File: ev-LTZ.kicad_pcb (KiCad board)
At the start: 2 copper layers, 50 x 100 mm, 41 parts, among them P1 VIN+, P2 CONN_01X02, P3 VH-, P4 VH+, P5 SENSE-, P6 SENSE+, P7 VIN-, Q1 BD139, U1 LT1013N8

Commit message: pcb
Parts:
- removed C8: 1uF, Capacitors_THT:CP_Radial_Tantal_D5.0mm_P5.00mm
- removed C9: .1uF, Capacitors_THT:C_Rect_L7.2mm_W2.5mm_P5.00mm_FKS2_FKP2_MKS2_MKP2
- removed D4, D5, D7: D_TVS, Diodes_THT:D_DO-15_P10.16mm_Horizontal
- C10, C5: value 1uF -> 47uF
- moved C4 83.9 mm to (137.1, 53.4), turned to 180 degrees
- moved C10 78.5 mm to (137.1, 58.0), turned to 180 degrees
- moved P2 77.3 mm to (134.0, 128.9), turned to 90 degrees
- moved TH1 63.5 mm to (142.9, 120.7), turned to 270 degrees
- moved D6 47.2 mm to (133.0, 87.8), turned to 270 degrees
- moved P4 42.5 mm to (134.0, 104.0)
- moved P6 38.5 mm to (175.9, 91.4)
- moved R4 36.8 mm to (168.9, 121.9)
- moved P7 33.9 mm to (176.5, 111.1)
- moved C5 29.6 mm to (155.0, 106.9), turned to 0 degrees
- moved P3 28.2 mm to (134.0, 116.8)
- moved P5 24.8 mm to (175.9, 78.7)
- moved P1 24.1 mm to (176.5, 123.8)
- moved W2 19.7 mm to (149.8, 129.0)
- moved D3 19.5 mm to (160.0, 126.4), turned to 0 degrees
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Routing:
- net Net-(C7-Pad1): track 30.6 -> 190.2 mm
- net Net-(LTZ1000-1-Pad4): track 75.2 -> 138.4 mm
- net Net-(C10-Pad1): track 98.5 -> 41.0 mm
- net /SENSE+: track 148.4 -> 203.9 mm
- net /VH-: track 134.0 -> 87.9 mm
- net Net-(C5-Pad1): track 63.0 -> 32.2 mm
- net /TSENSE: track 92.8 -> 114.6 mm
- net Net-(C2-Pad1): track 32.9 -> 48.1 mm
- net Net-(D2-Pad2): track 11.6 -> 24.6 mm
- net Net-(C1-Pad2): track 57.6 -> 44.7 mm
- net Net-(P2-Pad2): track 0.11 -> 10.2 mm
- net Net-(P2-Pad1): track 0.11 -> 8.94 mm
- net GND: track 198.4 -> 191.5 mm
- net /VH+: track 11.8 -> 6.62 mm
- net Net-(C3-Pad1): track 68.5 -> 71.8 mm
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
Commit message: V00 of pcb
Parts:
- moved D2 34.9 mm to (172.5, 99.7), turned to 180 degrees
- moved R9 16.2 mm to (159.6, 79.6), turned to 180 degrees
- moved LTZ1000-1 7.84 mm to (169.4, 57.7), turned to 270 degrees
- moved D1 6.36 mm to (146.7, 53.3)
- moved Q1 5.73 mm to (141.7, 57.9)
- moved R2 3.69 mm to (167.8, 118.6)
- moved W2 2.90 mm to (152.7, 129.0)
- moved R4 1.55 mm to (167.6, 122.8)
- moved P7 0.51 mm to (176.0, 111.1)
- moved P6 0.28 mm to (176.0, 91.2)
- moved P1 0.25 mm to (176.3, 123.8)
- moved R6 0.15 mm to (135.3, 82.5)
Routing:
- net Net-(C7-Pad1): track 190.2 -> 35.2 mm
- net Net-(LTZ1000-1-Pad4): track 138.4 -> 95.0 mm
- net Net-(C2-Pad1): track 48.1 -> 87.1 mm
- net GND: track 191.5 -> 160.1 mm
- net Net-(C3-Pad1): track 71.8 -> 101.3 mm
- net Net-(D2-Pad2): track 24.6 -> 4.37 mm
- net /SENSE+: track 203.9 -> 184.9 mm
- net Net-(C1-Pad2): track 44.7 -> 59.0 mm
- net /VH-: track 87.9 -> 81.9 mm
- net /HEAT: track 5.78 -> 11.0 mm
- net Net-(C5-Pad1): track 32.2 -> 36.9 mm
- net /TSENSE: track 114.6 -> 118.6 mm
- net Net-(C10-Pad1): track 41.0 -> 43.4 mm
- net Net-(D1-Pad2): track 20.2 -> 22.0 mm
- net Net-(C7-Pad2): track 32.8 -> 34.5 mm

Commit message: finish pcb
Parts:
- moved P3 49.8 mm to (133.6, 67.1)
- moved P4 26.3 mm to (133.6, 77.7)
- moved D6 23.3 mm to (137.7, 65.0)
- moved W1 11.0 mm to (145.8, 70.6)
- moved R6 9.34 mm to (143.3, 87.4)
- moved C1 8.32 mm to (138.2, 86.3)
- moved R7 6.88 mm to (138.2, 102.1)
- moved C4 5.61 mm to (138.2, 58.9), turned to 90 degrees
- moved R9 4.70 mm to (159.6, 84.3)
- moved P2 4.45 mm to (134.0, 124.5)
- moved R4 4.40 mm to (170.7, 126.0)
- moved TH1 4.32 mm to (142.9, 125.0)
- moved D3 3.68 mm to (160.0, 130.0)
- moved D2 3.06 mm to (174.8, 101.7)
- moved C10 3.02 mm to (136.7, 61.0)
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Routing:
- net /VH-: track 81.9 -> 25.2 mm
- net Net-(C10-Pad1): track 43.4 -> 19.1 mm
- net Net-(LTZ1000-1-Pad4): track 95.0 -> 118.7 mm
- net Net-(C7-Pad2): track 34.5 -> 20.4 mm
- net Net-(C3-Pad1): track 101.3 -> 110.7 mm
- net Net-(C2-Pad1): track 87.1 -> 79.1 mm
- net /SENSE+: track 184.9 -> 192.5 mm
- net Net-(C1-Pad2): track 59.0 -> 64.5 mm
- net /TSENSE: track 118.6 -> 115.1 mm
- net Net-(C1-Pad1): track 6.49 -> 3.08 mm
- net Net-(C5-Pad1): track 36.9 -> 33.7 mm
- net GND: track 160.1 -> 162.4 mm
- net Net-(D2-Pad2): track 4.37 -> 6.65 mm
- net /HEAT: track 11.0 -> 13.1 mm
- net /VH+: track 6.62 -> 5.12 mm
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- added copper zone on B.Cu, net /SENSE+
- added copper zone on F.Cu, net /SENSE+
- added copper zone on B.Cu, net /TSENSE
- added copper zone on B.Cu, net /VH-
- added copper zone on B.Cu, net /VIN+
- added copper zone on F.Cu, net GND
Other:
- net class Default: trace_width 0.508 -> 0.762
- net class Power added: clearance 0.2, trace_width 1.016, via_dia 0.6, via_drill 0.4

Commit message: change footprint
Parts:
- removed R4.2: 25k, Resistors_THT:R_Axial_DIN0614_L14.3mm_D5.7mm_P15.24mm_Horizontal
- R1, R2, R3, R5: footprint Resistors_THT:R_Axial_DIN0614_L14.3mm_D5.7mm_P15.24mm_Horizontal -> Resistors_THT:R_Axial_DIN0617_L17.0mm_D6.0mm_P20.32mm_Horizontal
- R4.1: value 25k -> 12k; footprint Resistors_THT:R_Axial_DIN0614_L14.3mm_D5.7mm_P15.24mm_Horizontal -> Resistors_THT:R_Axial_DIN0617_L17.0mm_D6.0mm_P20.32mm_Horizontal
- moved R1 60.6 mm to (189.2, 83.8)
- moved R4.1 9.16 mm to (133.1, 136.7)
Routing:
- net Net-(LTZ1000-1-Pad4): track 118.7 -> 42.4 mm
- net /TSENSE: track 115.1 -> 108.8 mm

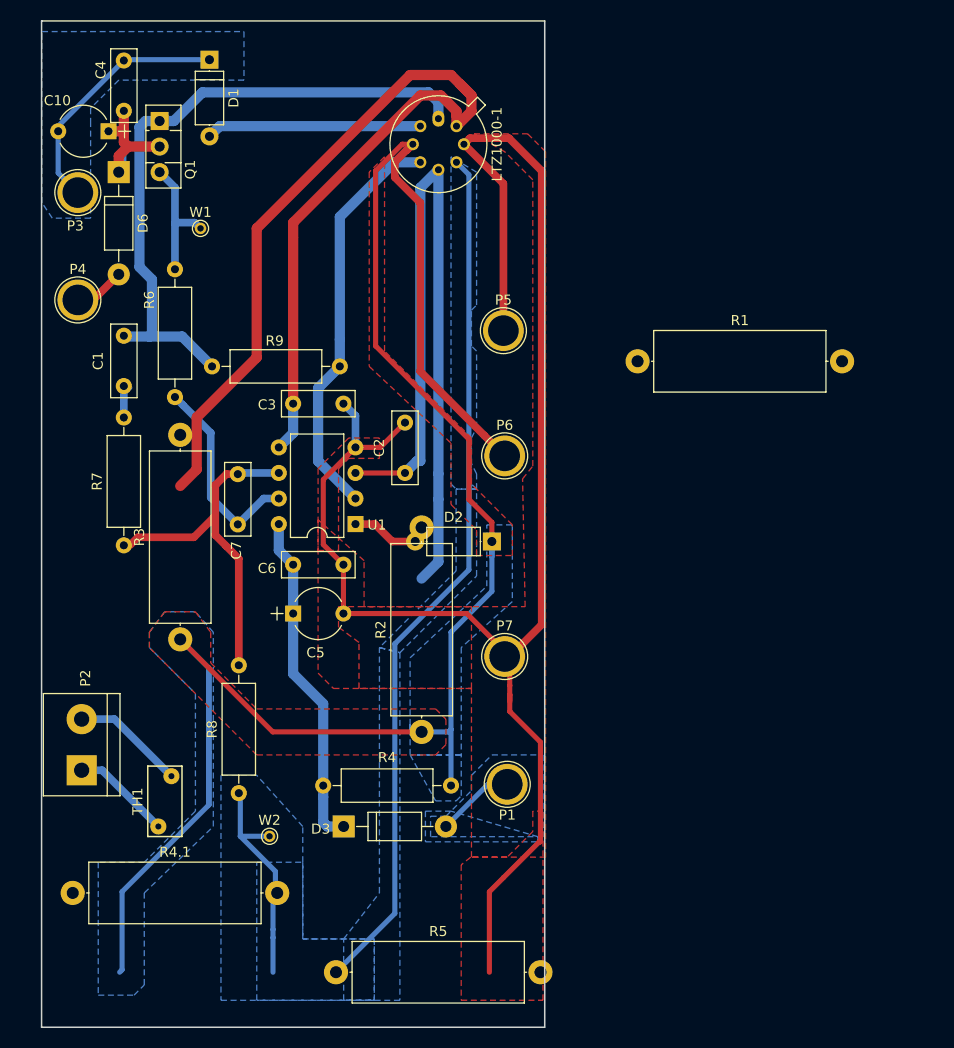
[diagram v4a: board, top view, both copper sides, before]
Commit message: modify layout
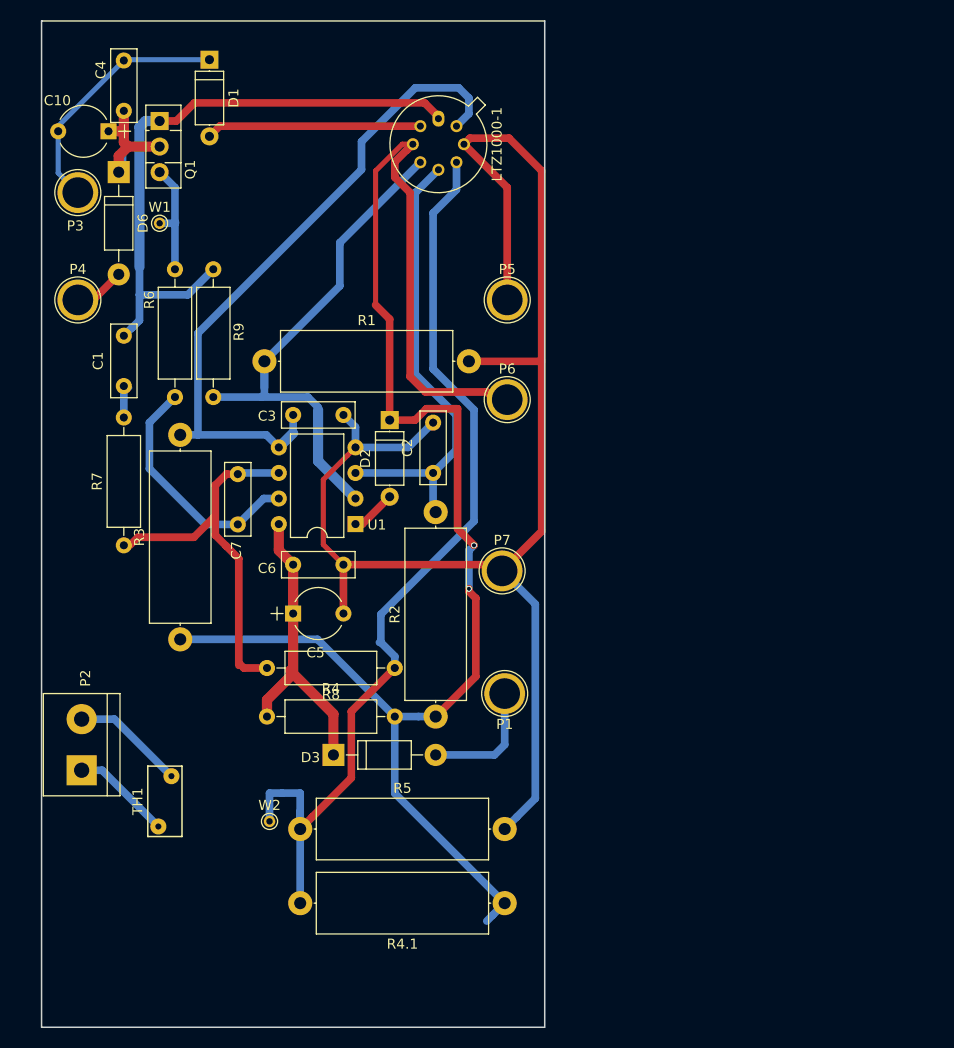
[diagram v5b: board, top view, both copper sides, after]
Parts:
- moved R4.1 42.9 mm to (176.0, 137.7), turned to 180 degrees
- moved R1 37.1 mm to (152.1, 83.8)
- moved R8 19.9 mm to (165.1, 114.3), turned to 180 degrees
- moved D2 15.8 mm to (164.6, 89.7), turned to 270 degrees
- moved R5 14.7 mm to (155.7, 130.3)
- moved R9 12.9 mm to (147.1, 87.4), turned to 90 degrees
- moved P1 9.02 mm to (176.0, 116.8)
- moved R4 8.85 mm to (165.1, 119.1)
- moved P7 8.51 mm to (175.8, 104.6)
- moved D3 7.18 mm to (159.0, 122.9)
- moved P6 5.59 mm to (176.3, 87.6)
- moved W1 4.10 mm to (141.7, 70.1)
- moved P5 3.07 mm to (176.3, 77.7)
- moved C2 2.79 mm to (168.9, 94.9)
- moved R2 2.07 mm to (169.2, 119.1)
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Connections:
- net /TSENSE renamed /TSENSE_B
- net Net-(C1-Pad2) renamed /HEATER+
- net Net-(C10-Pad1) renamed /VCC
- net Net-(C2-Pad1) renamed /TCOMP
- net Net-(C3-Pad1) renamed /TSENSE_C
- net Net-(D1-Pad2) renamed /HEATER-
- net Net-(D2-Pad2) renamed /CURRENT_OUT
- net Net-(LTZ1000-1-Pad4) renamed /ZENER-
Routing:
- net /TSENSE_C: track 110.7 -> 66.6 mm
- net /TCOMP: track 79.1 -> 45.4 mm
- net /SENSE+: track 192.5 -> 160.7 mm, vias 0 -> 2
- net /ZENER-: track 42.4 -> 55.8 mm
- net /TSENSE_B: track 108.8 -> 95.9 mm
- net GND: track 162.4 -> 151.2 mm
- net Net-(C7-Pad2): track 20.4 -> 24.4 mm
- net Net-(C7-Pad1): track 35.4 -> 38.4 mm
- net /HEATER+: track 64.5 -> 61.6 mm
- net Net-(C5-Pad1): track 33.7 -> 31.1 mm
- net /VIN+: track 9.72 -> 12.4 mm
- net /CURRENT_OUT: track 6.65 -> 4.52 mm
- net /HEAT: track 13.1 -> 11.9 mm
- added copper zone on B.Cu, net /TSENSE
- removed copper zone on B.Cu, net /SENSE+
- removed copper zone on F.Cu, net /SENSE+
- removed copper zone on B.Cu, net /TSENSE_B
- removed copper zone on B.Cu, net /VH-
- removed copper zone on B.Cu, net /VIN+
- removed copper zone on F.Cu, net GND

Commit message: improve traces
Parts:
- added R4.2: 25k, Resistors_THT:R_Axial_DIN0617_L17.0mm_D6.0mm_P20.32mm_Horizontal, F.Cu at (155.7, 120.7)
- added REF**: 1pin, Connectors:1pin, F.Cu at (157.4, 67.6)
- added REF**: 1pin, Connectors:1pin, F.Cu at (175.4, 60.2)
- C10, C5: footprint Capacitors_THT:CP_Radial_Tantal_D5.0mm_P5.00mm -> Capacitors_THT:CP_Radial_D8.0mm_P5.00mm
- P2: value CONN_01X02 -> TEMP NTC; footprint Connectors:bornier2 -> Connectors_Samtec:SL-102-X-XX_1x02
- P5, P6: footprint Connectors:1pin -> Measurement_Points:Measurement_Point_Round-TH_Big
- R4.1: value 12k -> 25k
- moved P3 77.6 mm to (136.0, 144.7)
- moved P4 69.0 mm to (149.7, 144.8)
- moved C10 54.9 mm to (138.0, 115.8)
- moved D6 54.3 mm to (140.5, 119.3)
- moved P7 40.3 mm to (174.0, 144.9)
- moved P1 31.0 mm to (162.7, 144.8)
- moved R2 27.2 mm to (172.7, 92.2), turned to 270 degrees
- moved C3 23.3 mm to (144.5, 110.0), turned to 270 degrees
- moved R4.1 23.0 mm to (155.7, 127.0), turned to 0 degrees
- moved W2 22.3 mm to (167.6, 113.0)
- moved R3 22.0 mm to (140.7, 89.7), turned to 270 degrees
- moved C1 21.3 mm to (138.4, 64.9)
- moved R5 20.5 mm to (176.0, 133.3), turned to 180 degrees
- moved R9 15.0 mm to (146.1, 72.4)
- moved W1 14.3 mm to (143.3, 84.3)
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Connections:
- net /VCC renamed /VCCH
- net Net-(C5-Pad1) renamed /VCCOPAMP
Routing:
- net GND: track 151.2 -> 233.0 mm
- net /VH-: track 25.2 -> 96.9 mm
- net /TSENSE_C: track 66.6 -> 127.2 mm
- net /VCCH: track 19.1 -> 72.0 mm
- net Net-(C1-Pad1): track 3.08 -> 33.6 mm
- net /VH+: track 5.12 -> 20.0 mm
- net /TCOMP: track 45.4 -> 59.8 mm
- net Net-(C7-Pad2): track 24.4 -> 12.1 mm
- net /HEAT: track 11.9 -> 24.0 mm
- net /HEATER+: track 61.6 -> 49.6 mm
- net /VIN+: track 12.4 -> 23.1 mm
- net /TSENSE_B: track 95.9 -> 86.3 mm
- net Net-(C7-Pad1): track 38.4 -> 46.5 mm
- net /SENSE+: track 160.7 -> 154.2 mm, vias 2 -> 0
- net /ZENER-: track 55.8 -> 50.8 mm
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- added copper zone on F.Cu, net (none)
- added copper zone on B.Cu, net /VH-
- added copper zone on B.Cu, net /ZENER-
- added copper zone on B.Cu, net GND
- removed copper zone on B.Cu, net /TSENSE

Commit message: change layout
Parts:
- C10, C5: footprint Capacitors_THT:CP_Radial_D8.0mm_P5.00mm -> Capacitors_THT:CP_Radial_D6.3mm_P2.50mm
- moved R7 27.2 mm to (138.3, 82.9)
- moved P5 26.7 mm to (175.9, 104.1)
- moved P6 26.7 mm to (175.9, 109.2)
- moved C2 6.15 mm to (165.1, 103.6), turned to 180 degrees
- moved TH1 4.18 mm to (143.4, 140.1)
- moved D6 3.45 mm to (138.4, 122.0)
- moved D2 3.31 mm to (164.5, 92.5)
- moved R2 3.06 mm to (169.7, 92.5)
- moved C6 2.88 mm to (152.1, 103.6)
- moved W2 2.74 mm to (165.1, 114.0)
- moved C5 2.60 mm to (151.3, 114.8), turned to 270 degrees
- moved R4.1 2.22 mm to (153.5, 127.1)
- moved R4.2 2.22 mm to (153.5, 120.6)
- moved R5 2.17 mm to (173.9, 133.5)
- moved REF** 1.22 mm to (158.4, 67.0)
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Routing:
- net Net-(C1-Pad1): track 33.6 -> 5.34 mm
- net /SENSE+: track 154.2 -> 169.9 mm
- net /TSENSE_C: track 127.2 -> 111.9 mm
- net GND: track 233.0 -> 246.5 mm
- net Net-(C7-Pad1): track 46.5 -> 52.1 mm
- net Net-(P2-Pad2): track 7.77 -> 12.3 mm
- net Net-(P2-Pad1): track 8.58 -> 12.6 mm
- net /TCOMP: track 59.8 -> 56.3 mm
- net /CURRENT_OUT: track 6.64 -> 3.30 mm
- net /VH-: track 96.9 -> 99.4 mm
- net /ZENER-: track 50.8 -> 52.5 mm
- net /HEAT: track 24.0 -> 25.2 mm
- net /VCCOPAMP: track 27.4 -> 26.3 mm
- net /VH+: track 20.0 -> 20.7 mm
- net /TSENSE_B: track 86.3 -> 85.7 mm
- removed copper zone on B.Cu, net /ZENER-
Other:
- board text added: "LTZ1000 +7V Reference"
- board text added: "Q"
- board text added: "X"
